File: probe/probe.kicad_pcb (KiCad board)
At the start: 2 copper layers, 21.5 x 13 mm, 4 parts, among them J1 To circuit, J2 To scope

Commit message: Update based on first constructed version
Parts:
- added C2: 5pF, Capacitor_SMD:C_0805_2012Metric, F.Cu at (147.1, 98.3)
- added R2: 4.5MΩ, Resistor_SMD:R_0805_2012Metric_Pad1.20x1.40mm_HandSolder, F.Cu at (149.1, 92.0)
- R1: value 9MΩ -> 4.5MΩ
- moved R1 2.44 mm to (144.9, 92.0)
- moved C1 1.85 mm to (147.0, 95.0)
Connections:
- net Net-(J1-In) renamed /In
- C1 pad 2: Net-(J2-In) -> /Out
- J2 pad 1: Net-(J2-In) -> /Out
- R1 pad 2: Net-(J2-In) -> Net-(R1-Pad2)
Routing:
- net Net-(J2-In): track 10.7 -> 0.00 mm
- net /In: track 11.2 -> 0.67 mm
- net Net-(R1-Pad2): track 0.00 -> 2.20 mm
- net GND: vias 0 -> 4
- added copper zone on F.Cu, net /In
- added copper zone on F.Cu, net /Out

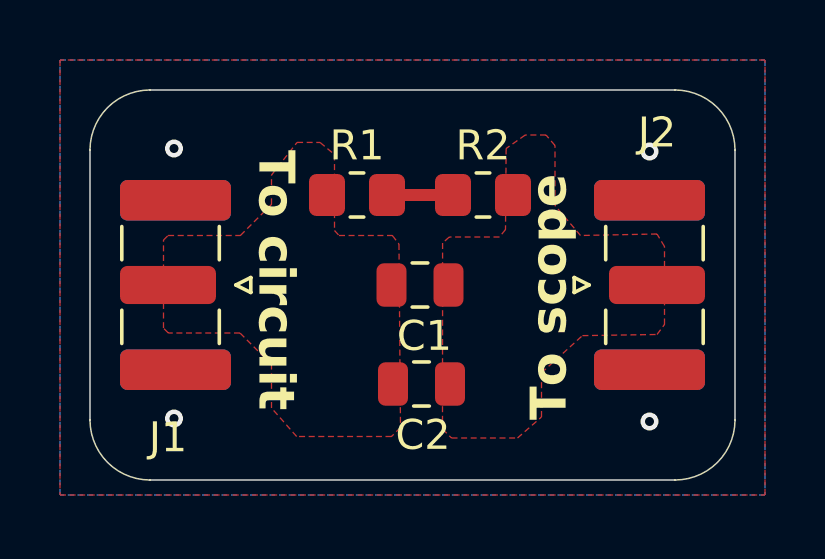
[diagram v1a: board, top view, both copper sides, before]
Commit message: Combined both boards into single probe board
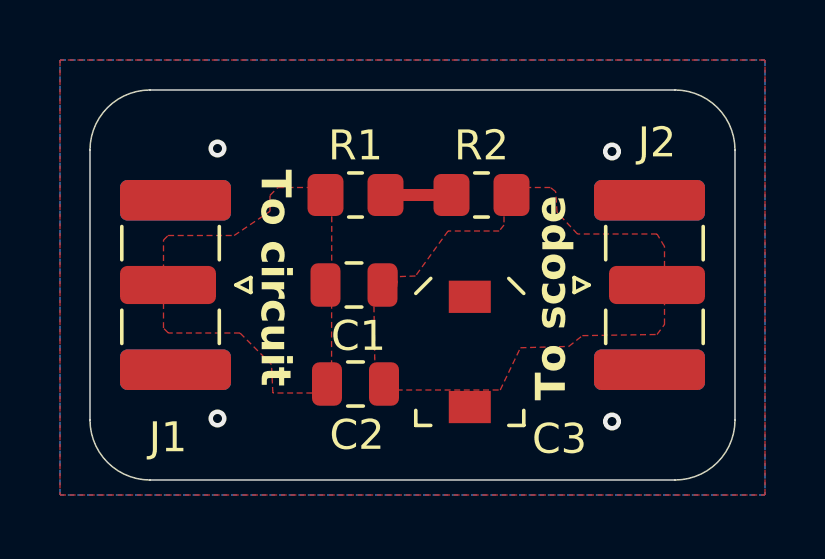
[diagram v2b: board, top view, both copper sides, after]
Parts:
- added C3: 8-30pF, Capacitor_SMD:C_Trimmer_Sprague-Goodman_SGC3, F.Cu at (148.7, 97.2)
- moved C2 2.20 mm to (144.8, 98.3)
- moved C1 2.20 mm to (144.8, 95.0)
- moved R1 0.05 mm to (144.8, 92.0)
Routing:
- net /In: track 0.67 -> 0.00 mm

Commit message: Latest PCB design
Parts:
- added G***: LOGO, Symbol:qr, F.Cu at (146.3, 95.8)
